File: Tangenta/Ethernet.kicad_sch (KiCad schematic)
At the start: 31 parts, among them J20 Conn_01x08_Pin, U18 RTL8367S-CG, X2 X322525MOB4SI

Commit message: Ethernet hierarchy continued.
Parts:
- removed C1 (x11): 100nF, Capacitor_SMD:C_0402_1005Metric, symbol Device:C_Small
- removed C1 (x2): 18pF, Capacitor_SMD:C_0402_1005Metric, symbol Device:C_Small
- removed C1 (x2): 10uF, Capacitor_SMD:C_0402_1005Metric, symbol Device:C_Small
- removed J20: Conn_01x08_Pin, Connector_PinHeader_1.00mm:PinHeader_1x08_P1.00mm_Vertical, symbol Connector:Conn_01x08_Pin
- removed R2: 1M, Resistor_SMD:R_0402_1005Metric, symbol Device:R_Small_US
- removed R4 (x5): 4.7k, Resistor_SMD:R_0603_1608Metric, symbol Device:R_Small_US
- removed R4 (x6): 1k, Resistor_SMD:R_0603_1608Metric, symbol Device:R_Small_US
- removed R4: 2.49k 1%, Resistor_SMD:R_0603_1608Metric, symbol Device:R_Small_US
- removed U18: RTL8367S-CG, RTL8367S_CG:RTL8367S-CG, symbol RTL8367S_CG:RTL8367S-CG
- removed X2: X322525MOB4SI, XTAL_25MHZ:XTAL_25MHZ, symbol XTAL_25MHZ:X322525MOB4SI
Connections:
- no-connect marks 11 -> 0
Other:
- added sheet Ethernet_Switch (Ethernet_Switch.kicad_sch)

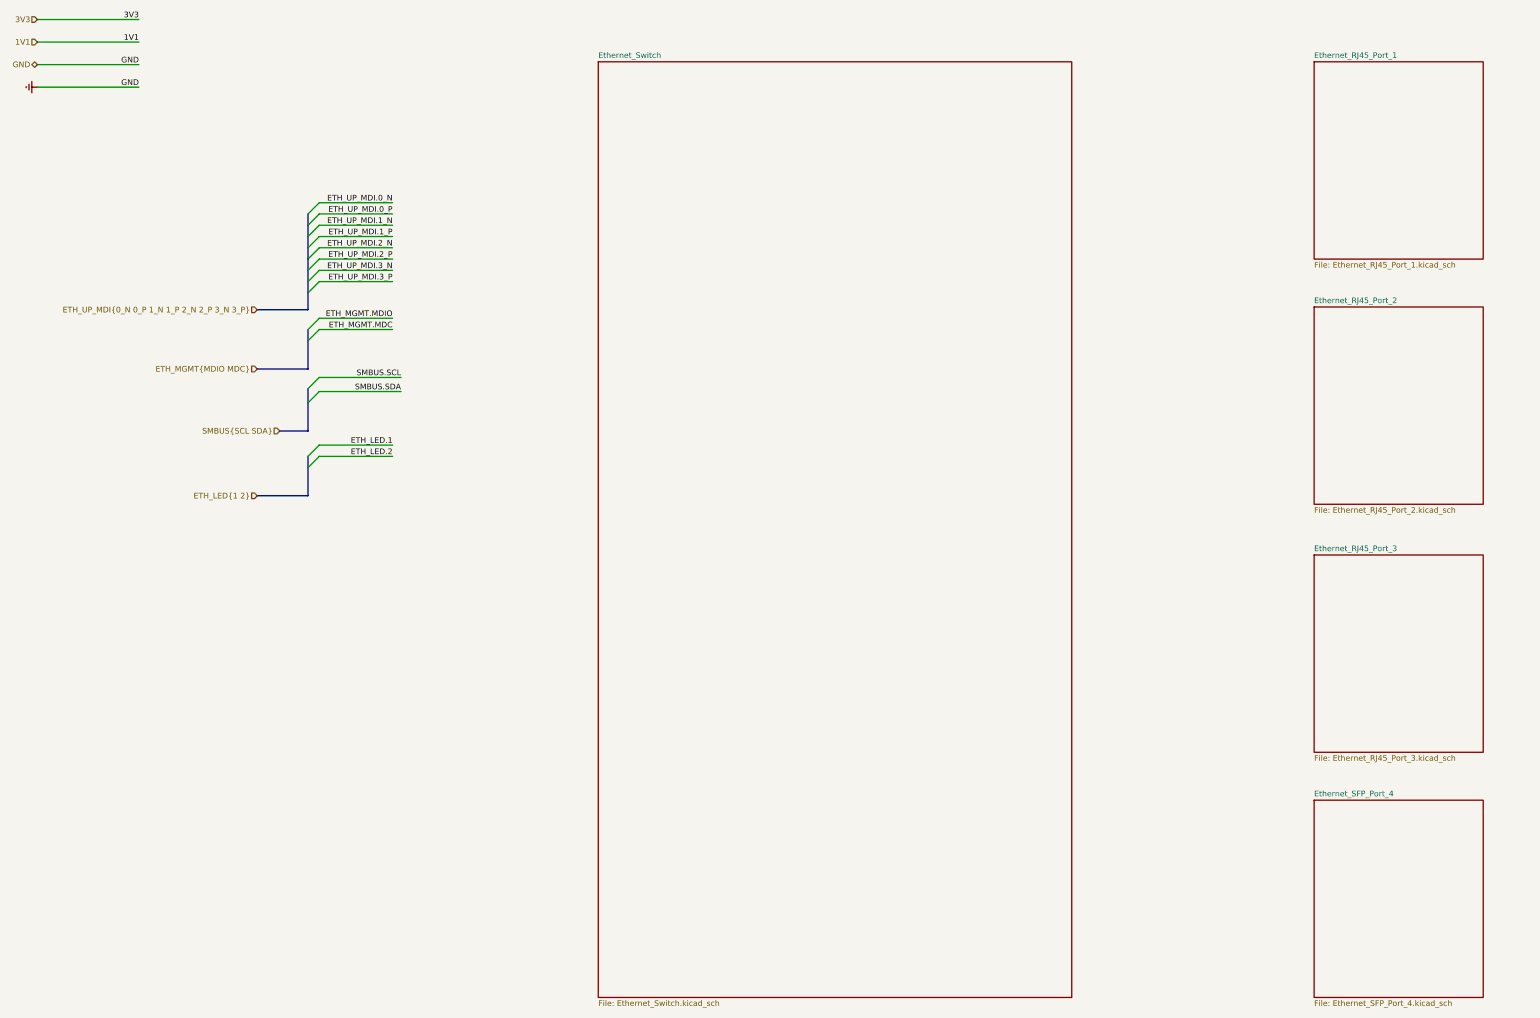
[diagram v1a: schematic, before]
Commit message: Ethernet Switch schematic done, ports TBD...
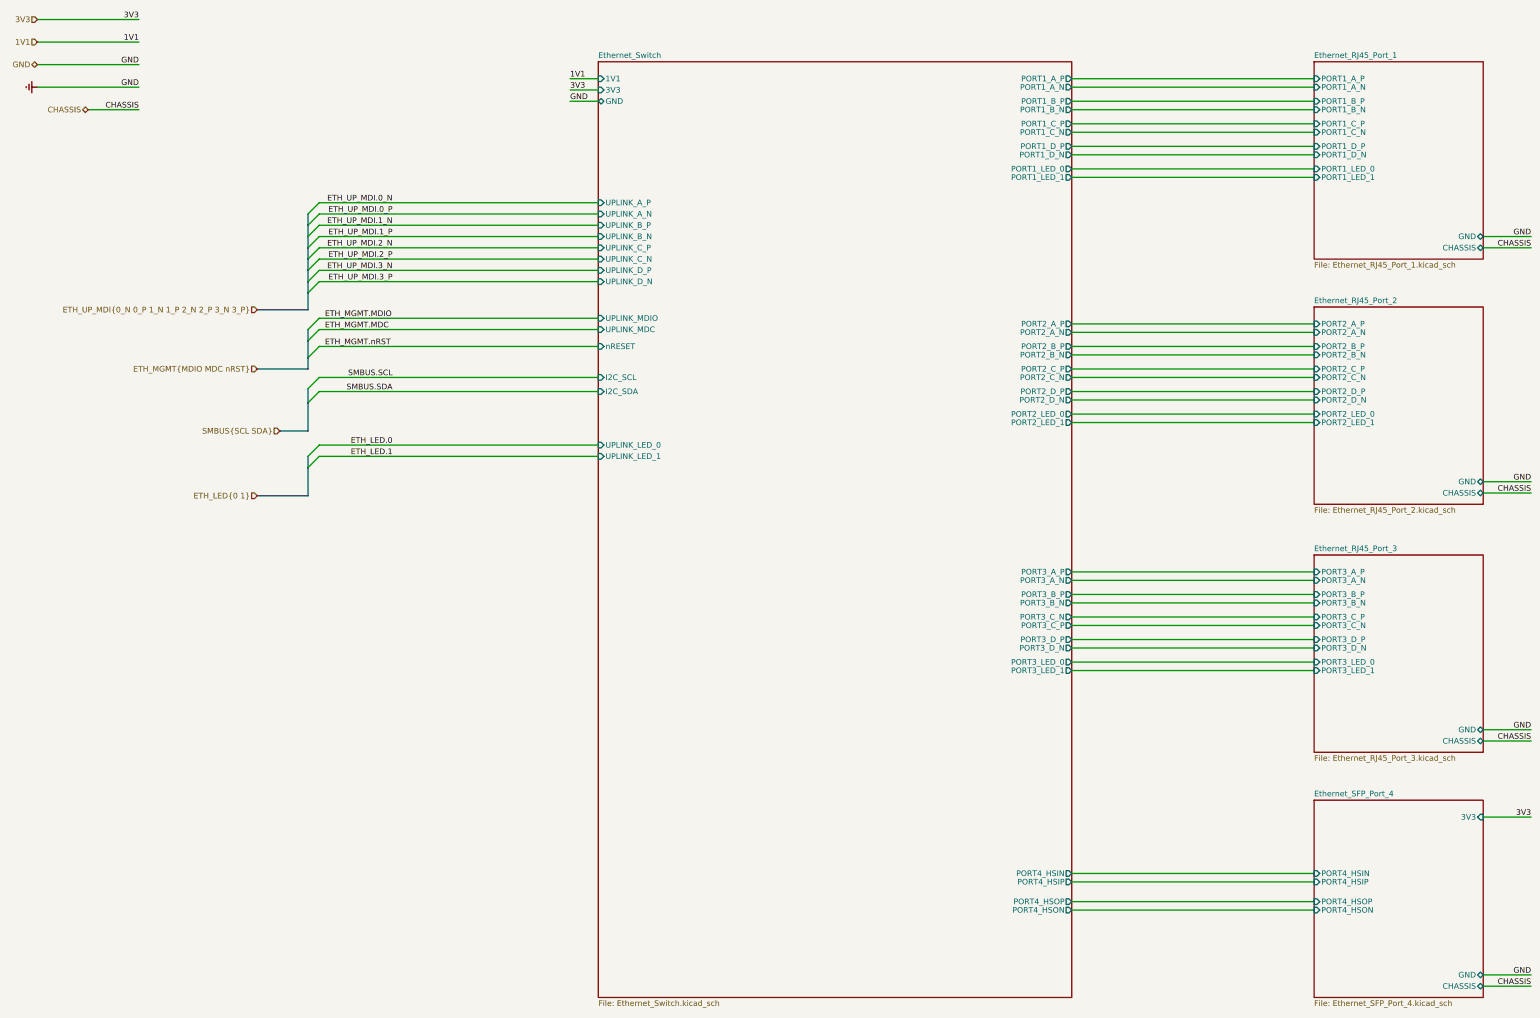
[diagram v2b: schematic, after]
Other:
- sheet Ethernet_RJ45_Port_1 ports: added CHASSIS, GND, PORT1_A_N, PORT1_A_P, PORT1_B_N, PORT1_B_P, PORT1_C_N, PORT1_C_P, PORT1_D_N, PORT1_D_P, PORT1_LED_0, PORT1_LED_1; removed none
- sheet Ethernet_RJ45_Port_2 ports: added CHASSIS, GND, PORT2_A_N, PORT2_A_P, PORT2_B_N, PORT2_B_P, PORT2_C_N, PORT2_C_P, PORT2_D_N, PORT2_D_P, PORT2_LED_0, PORT2_LED_1; removed none
- sheet Ethernet_RJ45_Port_3 ports: added CHASSIS, GND, PORT3_A_N, PORT3_A_P, PORT3_B_N, PORT3_B_P, PORT3_C_N, PORT3_C_P, PORT3_D_N, PORT3_D_P, PORT3_LED_0, PORT3_LED_1; removed none
- sheet Ethernet_SFP_Port_4 ports: added 3V3, CHASSIS, GND, PORT4_HSIN, PORT4_HSIP, PORT4_HSON, PORT4_HSOP; removed none
- sheet Ethernet_Switch ports: added 1V1, 3V3, GND, I2C_SCL, I2C_SDA, PORT1_A_N, PORT1_A_P, PORT1_B_N, PORT1_B_P, PORT1_C_N, PORT1_C_P, PORT1_D_N, PORT1_D_P, PORT1_LED_0, PORT1_LED_1, PORT2_A_N, PORT2_A_P, PORT2_B_N, PORT2_B_P, PORT2_C_N, PORT2_C_P, PORT2_D_N, PORT2_D_P, PORT2_LED_0, PORT2_LED_1, PORT3_A_N, PORT3_A_P, PORT3_B_N, PORT3_B_P, PORT3_C_N, PORT3_C_P, PORT3_D_N, PORT3_D_P, PORT3_LED_0, PORT3_LED_1, PORT4_HSIN, PORT4_HSIP, PORT4_HSON, PORT4_HSOP, UPLINK_A_N, UPLINK_A_P, UPLINK_B_N, UPLINK_B_P, UPLINK_C_N, UPLINK_C_P, UPLINK_D_N, UPLINK_D_P, UPLINK_LED_0, UPLINK_LED_1, UPLINK_MDC, UPLINK_MDIO, nRESET; removed none

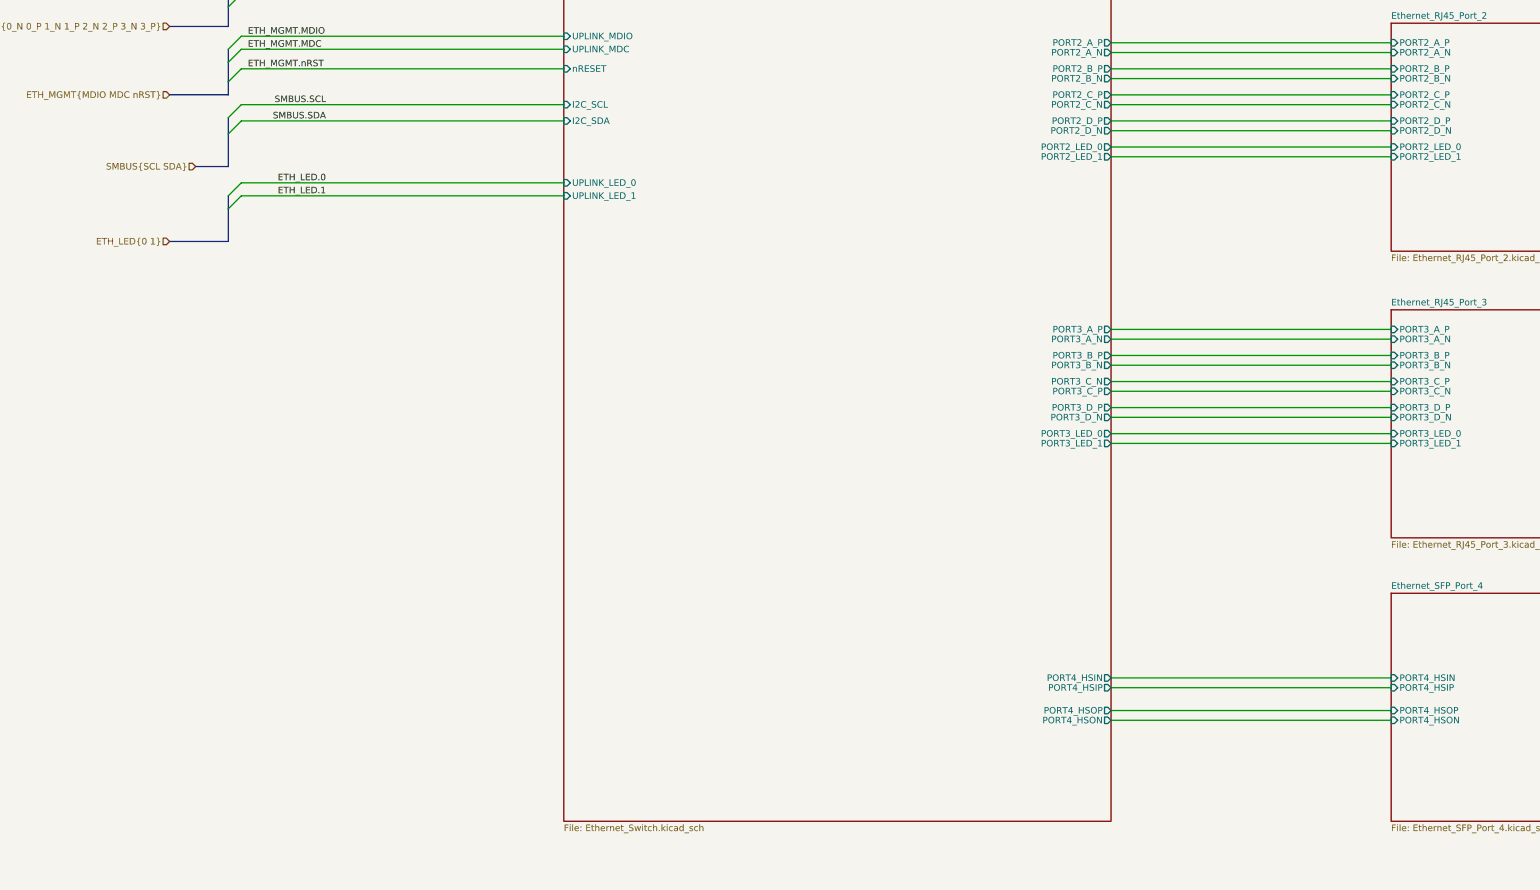
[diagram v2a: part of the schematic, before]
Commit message: Ethernet ready for routing.
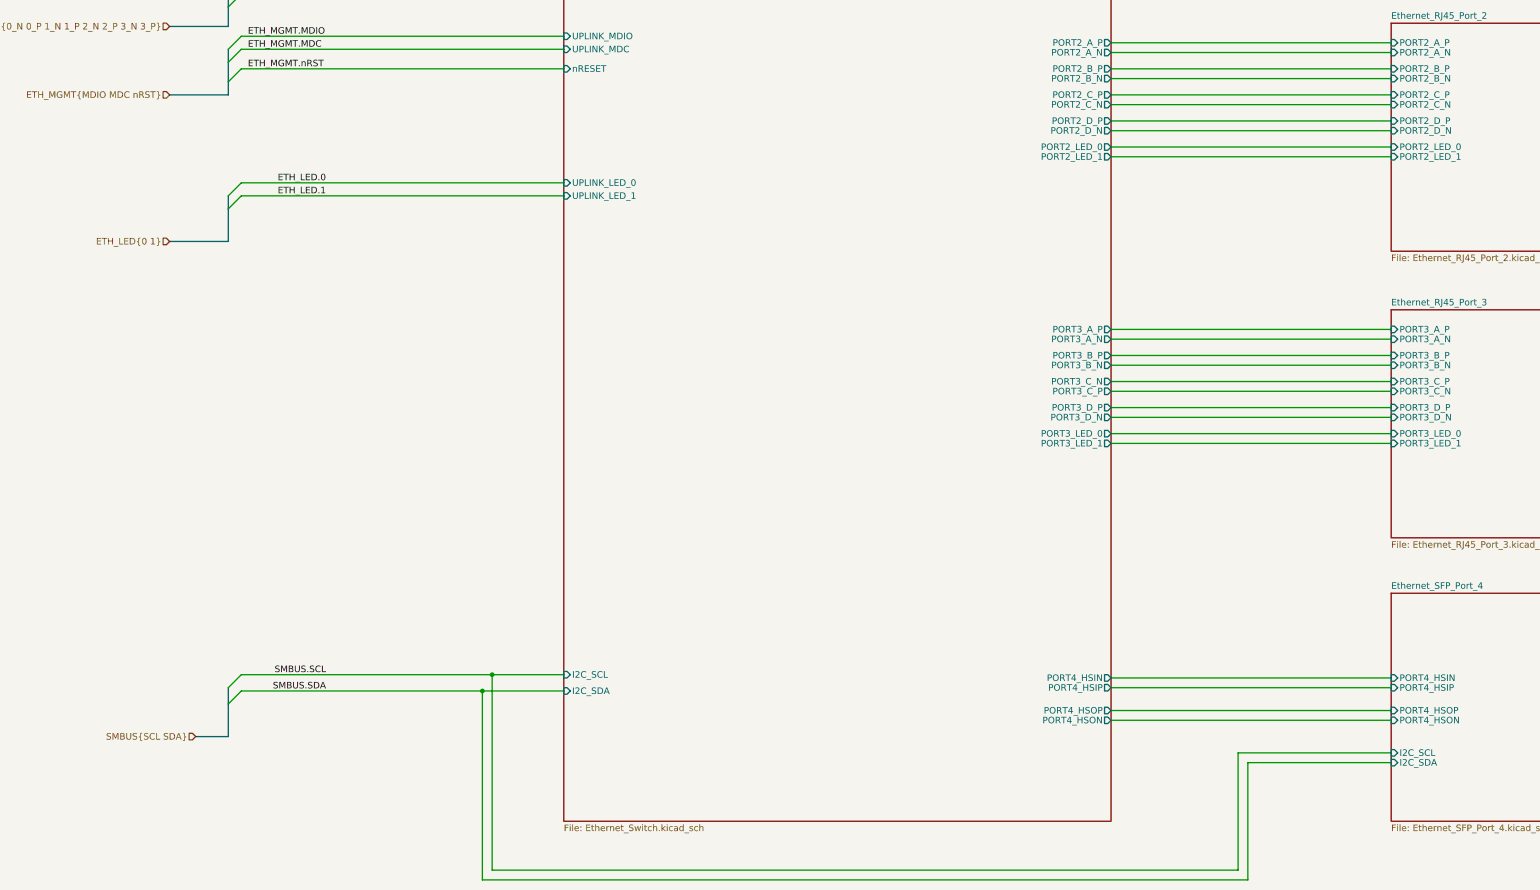
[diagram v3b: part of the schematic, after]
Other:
- sheet Ethernet_SFP_Port_4 ports: added I2C_SCL, I2C_SDA; removed none
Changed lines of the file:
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@@
 (kicad_sch (version 20230121) (generator eeschema)
   (paper "A3")
-  (bus_entry (at 80.01 102.87) (size 2.54 -2.54)
+  (junction (at 129.54 214.63) (diameter 0) (color 0 0 0 0)
+  )
+  (junction (at 131.445 211.455) (diameter 0) (color 0 0 0 0)
+  )
+  (bus_entry (at 80.01 213.995) (size 2.54 -2.54)
     (stroke (width 0) (type default))
   )
@@
     (stroke (width 0) (type default))
   )
-  (bus_entry (at 80.01 106.045) (size 2.54 -2.54)
+  (bus_entry (at 80.01 217.17) (size 2.54 -2.54)
     (stroke (width 0) (type default))
   )
@@
     (stroke (width 0) (type default))
   )
+  (wire (pts (xy 306.705 228.6) (xy 278.765 228.6))
+    (stroke (width 0) (type default))
+  )
   (wire (pts (xy 82.55 68.58) (xy 145.415 68.58))
     (stroke (width 0) (type default))
@@
     (stroke (width 0) (type default))
   )
+  (wire (pts (xy 131.445 249.555) (xy 276.86 249.555))
+    (stroke (width 0) (type default))
+  )
   (wire (pts (xy 344.805 71.12) (xy 355.6 71.12))
     (stroke (width 0) (type default))
   )
+  (wire (pts (xy 129.54 251.46) (xy 129.54 214.63))
+    (stroke (width 0) (type default))
+  )
   (wire (pts (xy 82.55 71.12) (xy 145.415 71.12))
     (stroke (width 0) (type default))
@@
     (stroke (width 0) (type default))
   )
-  (wire (pts (xy 82.55 103.505) (xy 145.415 103.505))
+  (wire (pts (xy 82.55 214.63) (xy 129.54 214.63))
     (stroke (width 0) (type default))
   )
@@
     (stroke (width 0) (type default))
   )
-  (bus (pts (xy 80.01 106.045) (xy 80.01 112.395))
+  (wire (pts (xy 278.765 251.46) (xy 129.54 251.46))
+    (stroke (width 0) (type default))
+  )
+  (bus (pts (xy 80.01 217.17) (xy 80.01 223.52))
     (stroke (width 0) (type default))
   )
@@
     (stroke (width 0) (type default))
   )
+  (wire (pts (xy 276.86 226.695) (xy 306.705 226.695))
+    (stroke (width 0) (type default))
+  )
   (wire (pts (xy 252.095 43.18) (xy 306.705 43.18))
     (stroke (width 0) (type default))
@@
     (stroke (width 0) (type default))
   )
-  (bus (pts (xy 80.01 102.87) (xy 80.01 106.045))
+  (bus (pts (xy 80.01 213.995) (xy 80.01 217.17))
     (stroke (width 0) (type default))
   )
@@
     (stroke (width 0) (type default))
   )
+  (wire (pts (xy 278.765 228.6) (xy 278.765 251.46))
+    (stroke (width 0) (type default))
+  )
   (bus (pts (xy 68.58 98.425) (xy 80.01 98.425))
     (stroke (width 0) (type default))
@@
     (stroke (width 0) (type default))
   )
-  (wire (pts (xy 82.55 100.33) (xy 145.415 100.33))
+  (wire (pts (xy 82.55 211.455) (xy 131.445 211.455))
     (stroke (width 0) (type default))
   )
@@
     (stroke (width 0) (type default))
   )
+  (wire (pts (xy 129.54 214.63) (xy 145.415 214.63))
+    (stroke (width 0) (type default))
+  )
   (wire (pts (xy 82.55 73.66) (xy 145.415 73.66))
     (stroke (width 0) (type default))
@@
     (stroke (width 0) (type default))
   )
+  (wire (pts (xy 131.445 211.455) (xy 131.445 249.555))
+    (stroke (width 0) (type default))
+  )
   (wire (pts (xy 252.095 105.41) (xy 306.705 105.41))
     (stroke (width 0) (type default))
   )
-  (bus (pts (xy 73.66 112.395) (xy 80.01 112.395))
+  (bus (pts (xy 73.66 223.52) (xy 80.01 223.52))
     (stroke (width 0) (type default))
   )
@@
     (stroke (width 0) (type default))
   )
+  (wire (pts (xy 131.445 211.455) (xy 145.415 211.455))
+    (stroke (width 0) (type default))
+  )
   (wire (pts (xy 252.095 45.085) (xy 306.705 45.085))
     (stroke (width 0) (type default))
@@
   )
   (bus (pts (xy 80.01 118.11) (xy 80.01 120.65))
+    (stroke (width 0) (type default))
+  )
+  (wire (pts (xy 276.86 249.555) (xy 276.86 226.695))
     (stroke (width 0) (type default))
   )
@@
     (effects (font (size 1.27 1.27)) (justify right bottom))
   )
-  (label "SMBUS.SCL" (at 99.06 100.33 180) (fields_autoplaced)
+  (label "SMBUS.SCL" (at 99.06 211.455 180) (fields_autoplaced)
     (effects (font (size 1.27 1.27)) (justify right bottom))
   )
@@
     (effects (font (size 1.27 1.27)) (justify right bottom))
   )
-  (label "SMBUS.SDA" (at 99.06 103.505 180) (fields_autoplaced)
+  (label "SMBUS.SDA" (at 99.06 214.63 180) (fields_autoplaced)
     (effects (font (size 1.27 1.27)) (justify right bottom))
   )
@@
     (effects (font (size 1.27 1.27)) (justify right))
   )
-  (hierarchical_label "SMBUS{SCL SDA}" (shape input) (at 73.66 112.395 180) (fields_autoplaced)
+  (hierarchical_label "SMBUS{SCL SDA}" (shape input) (at 73.66 223.52 180) (fields_autoplaced)
     (effects (font (size 1.27 1.27)) (justify right))
   )
@@
       (effects (font (size 1.27 1.27)) (justify left))
     )
+    (pin "I2C_SCL" input (at 306.705 226.695 180)
+      (effects (font (size 1.27 1.27)) (justify left))
+    )
+    (pin "I2C_SDA" input (at 306.705 228.6 180)
+      (effects (font (size 1.27 1.27)) (justify left))
+    )
     (instances
       (project "Tangenta"
@@
       (effects (font (size 1.27 1.27)) (justify left))
     )
-    (pin "I2C_SDA" input (at 145.415 103.505 180)
-      (effects (font (size 1.27 1.27)) (justify left))
-    )
-    (pin "I2C_SCL" input (at 145.415 100.33 180)
-      (effects (font (size 1.27 1.27)) (justify left))
-    )
+    (pin "I2C_SDA" input (at 145.415 214.63 180)
+      (effects (font (size 1.27 1.27)) (justify left))
+    )
+    (pin "I2C_SCL" input (at 145.415 211.455 180)
+      (effects (font (size 1.27 1.27)) (justify left))
+    )
